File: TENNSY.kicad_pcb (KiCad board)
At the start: 2 copper layers, 120 x 160 mm, 3 parts, among them U1 Teensy4.0

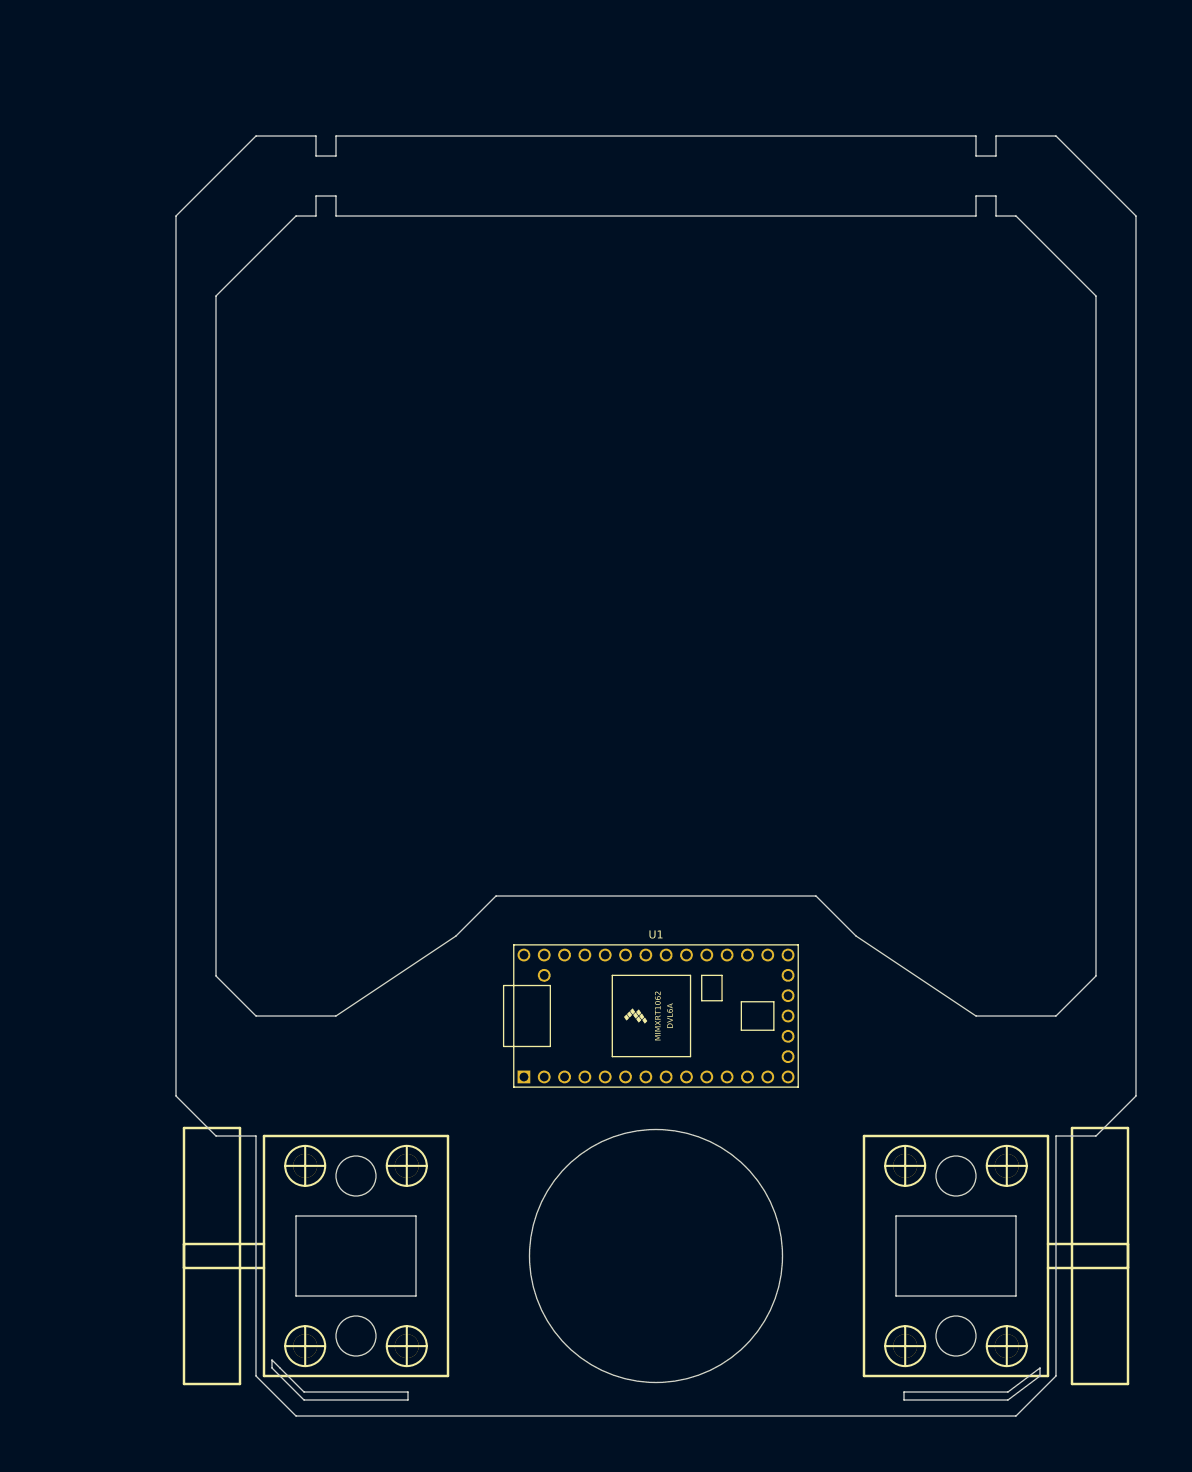
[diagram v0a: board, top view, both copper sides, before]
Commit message: modificaciones
se arego imagenes 3d y modificacion en el sch y pcb
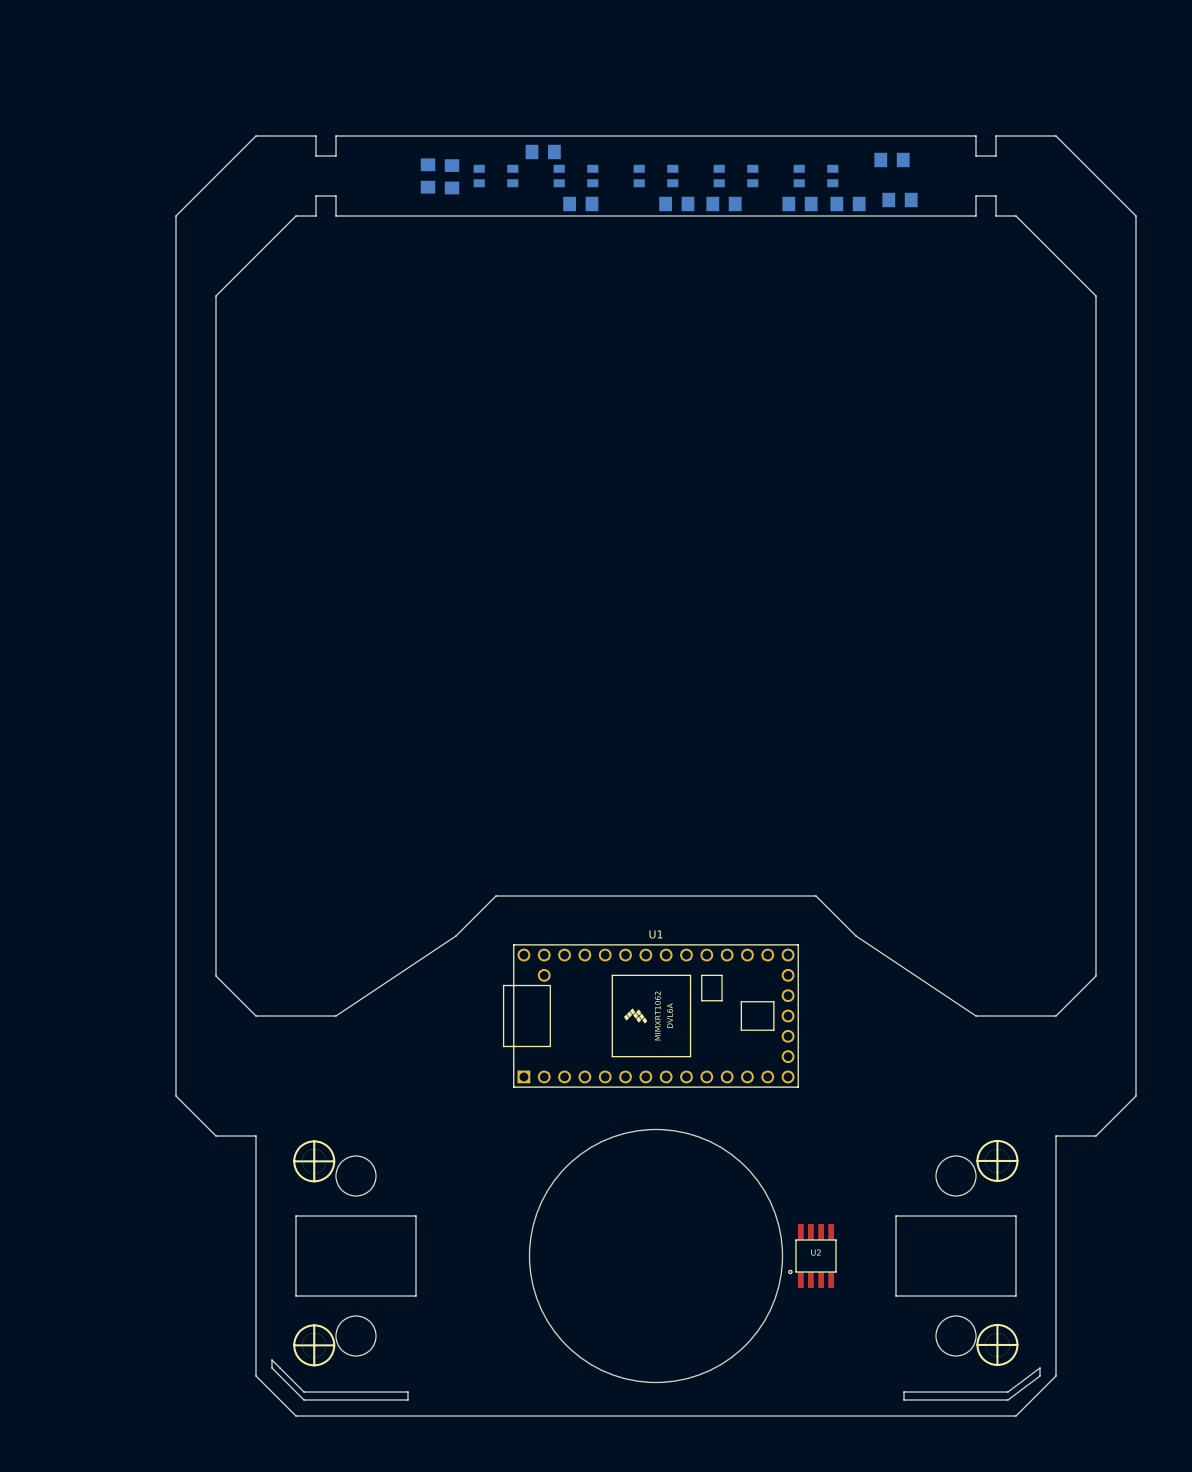
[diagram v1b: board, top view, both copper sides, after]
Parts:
- removed the Pololu_Micro_Gear_Motor at (127.5, 165.0)
- removed the Pololu_Micro_Gear_Motor at (52.5, 165.0)
- added Pololu_Micro_Gear_Motor: VAL**, EESTN5:Pololu_Micro_Con_Soporte_Simple, B.Cu at (47.3, 164.7)
- added Pololu_Micro_Gear_Motor: VAL**, EESTN5:Pololu_Micro_Con_Soporte_Simple, B.Cu at (132.7, 164.6)
- added R1: R, EESTN5:R_1206, B.Cu at (75.9, 27.0)
- added R10: R, EESTN5:R_1206, B.Cu at (120.5, 33.0)
- added R2: R, EESTN5:R_1206, B.Cu at (80.6, 33.5)
- added R3: R, EESTN5:R_1206, B.Cu at (64.5, 30.1)
- added R4: R, EESTN5:R_1206, B.Cu at (61.5, 30.0)
- added R5: R, EESTN5:R_1206, B.Cu at (98.5, 33.5)
- added R6: R, EESTN5:R_1206, B.Cu at (92.6, 33.5)
- added R7: R, EESTN5:R_1206, B.Cu at (114.0, 33.5)
- added R8: R, EESTN5:R_1206, B.Cu at (108.0, 33.5)
- added R9: R, EESTN5:R_1206, B.Cu at (119.5, 28.0)
- added U2: DRV8872, EESTN5:SSOP-8, F.Cu at (110.0, 165.0)
- added U3: QRE1113, EESTN5:QRE1113GR, B.Cu at (80.0, 30.0)
- added U4: QRE1113, EESTN5:QRE1113GR, B.Cu at (70.0, 30.0)
- added U5: QRE1113, EESTN5:QRE1113GR, B.Cu at (90.0, 30.0)
- added U6: QRE1113, EESTN5:QRE1113GR, B.Cu at (100.0, 30.0)
- added U7: QRE1113, EESTN5:QRE1113GR, B.Cu at (110.0, 30.0)
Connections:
- U1 pad 1: Net-(U1-Pad1) -> (no net)
- U1 pad 10: Net-(U1-Pad10) -> (no net)
- U1 pad 11: Net-(U1-Pad11) -> (no net)
- U1 pad 12: Net-(U1-Pad12) -> (no net)
- U1 pad 13: Net-(U1-Pad13) -> (no net)
- U1 pad 14: Net-(U1-Pad14) -> (no net)
- U1 pad 15: Net-(U1-Pad15) -> (no net)
- U1 pad 16: Net-(U1-Pad16) -> (no net)
- U1 pad 17: Net-(U1-Pad17) -> (no net)
- U1 pad 18: Net-(U1-Pad18) -> (no net)
- U1 pad 19: Net-(U1-Pad19) -> (no net)
- U1 pad 2: Net-(U1-Pad2) -> (no net)
- U1 pad 20: Net-(U1-Pad20) -> (no net)
- U1 pad 21: Net-(U1-Pad21) -> (no net)
- U1 pad 22: Net-(U1-Pad22) -> (no net)
- U1 pad 23: Net-(U1-Pad23) -> (no net)
- U1 pad 24: Net-(U1-Pad24) -> (no net)
- U1 pad 25: Net-(U1-Pad25) -> (no net)
- U1 pad 26: Net-(U1-Pad26) -> (no net)
- U1 pad 27: Net-(U1-Pad27) -> (no net)
- U1 pad 28: Net-(U1-Pad28) -> (no net)
- U1 pad 29: Net-(U1-Pad29) -> (no net)
- U1 pad 3: Net-(U1-Pad3) -> (no net)
- U1 pad 30: Net-(U1-Pad30) -> (no net)
- U1 pad 31: Net-(U1-Pad31) -> (no net)
- U1 pad 32: Net-(U1-Pad32) -> (no net)
- U1 pad 33: Net-(U1-Pad33) -> (no net)
- U1 pad 34: Net-(U1-Pad34) -> (no net)
- U1 pad 4: Net-(U1-Pad4) -> (no net)
- U1 pad 5: Net-(U1-Pad5) -> (no net)
- U1 pad 6: Net-(U1-Pad6) -> (no net)
- U1 pad 7: Net-(U1-Pad7) -> (no net)
- U1 pad 8: Net-(U1-Pad8) -> (no net)
- U1 pad 9: Net-(U1-Pad9) -> (no net)

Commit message: modificaciones
se modifico el pcb
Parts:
- R1, R10, R2, R3, R4, R5, R6, R7, R8, R9: moved to F.Cu
- moved R7 16.9 mm to (97.8, 28.6), turned to 90 degrees
- moved R5 11.8 mm to (87.8, 28.6), turned to 90 degrees
- moved R9 11.7 mm to (107.8, 28.6), turned to 90 degrees
- moved R4 10.8 mm to (72.2, 28.6)
- moved R10 9.57 mm to (112.0, 28.6), turned to 90 degrees
- moved R8 7.74 mm to (102.0, 28.6), turned to 90 degrees
- moved R2 5.09 mm to (82.0, 28.6), turned to 90 degrees
- moved R6 4.94 mm to (92.0, 28.6), turned to 90 degrees
- moved R3 3.45 mm to (67.6, 28.6)
- moved R1 2.49 mm to (77.8, 28.6), turned to 90 degrees
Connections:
- R10 pad 2: /5 -> /A0
- R2 pad 2: /2 -> /A3
- R4 pad 2: /1 -> /A6
- R6 pad 2: /3 -> /A2
- R8 pad 2: /4 -> /A1
- U1 pad 1: (no net) -> GND
- U1 pad 17: (no net) -> GND
- U1 pad 21: (no net) -> /A0
- U1 pad 22: (no net) -> /A1
- U1 pad 23: (no net) -> /A2
- U1 pad 24: (no net) -> /A3
- U1 pad 27: (no net) -> /A6
- U1 pad 32: (no net) -> GND
- U3 pad 3: /2 -> /A3
- U4 pad 3: /1 -> /A6
- U5 pad 3: /3 -> /A2
- U6 pad 3: /4 -> /A1
- U7 pad 3: /5 -> /A0
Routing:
- net /A3: track 0.00 -> 226.9 mm, vias 0 -> 1
- net /A2: track 0.00 -> 217.3 mm, vias 0 -> 1
- net /A6: track 0.00 -> 213.5 mm, vias 0 -> 1
- net /A1: track 0.00 -> 207.7 mm, vias 0 -> 1
- net /A0: track 0.00 -> 198.8 mm, vias 0 -> 1
- net +5V: track 0.00 -> 44.4 mm
- net Net-(R7-Pad2): track 0.00 -> 5.62 mm, vias 0 -> 1
- net Net-(R9-Pad2): track 0.00 -> 5.39 mm, vias 0 -> 1
- net Net-(R1-Pad2): track 0.00 -> 5.20 mm, vias 0 -> 1
- net Net-(R3-Pad2): track 0.00 -> 4.96 mm, vias 0 -> 1
- net Net-(R5-Pad2): track 0.00 -> 4.87 mm, vias 0 -> 1
- added copper zone on B.Cu, net GND
- added copper zone on F.Cu, net GND

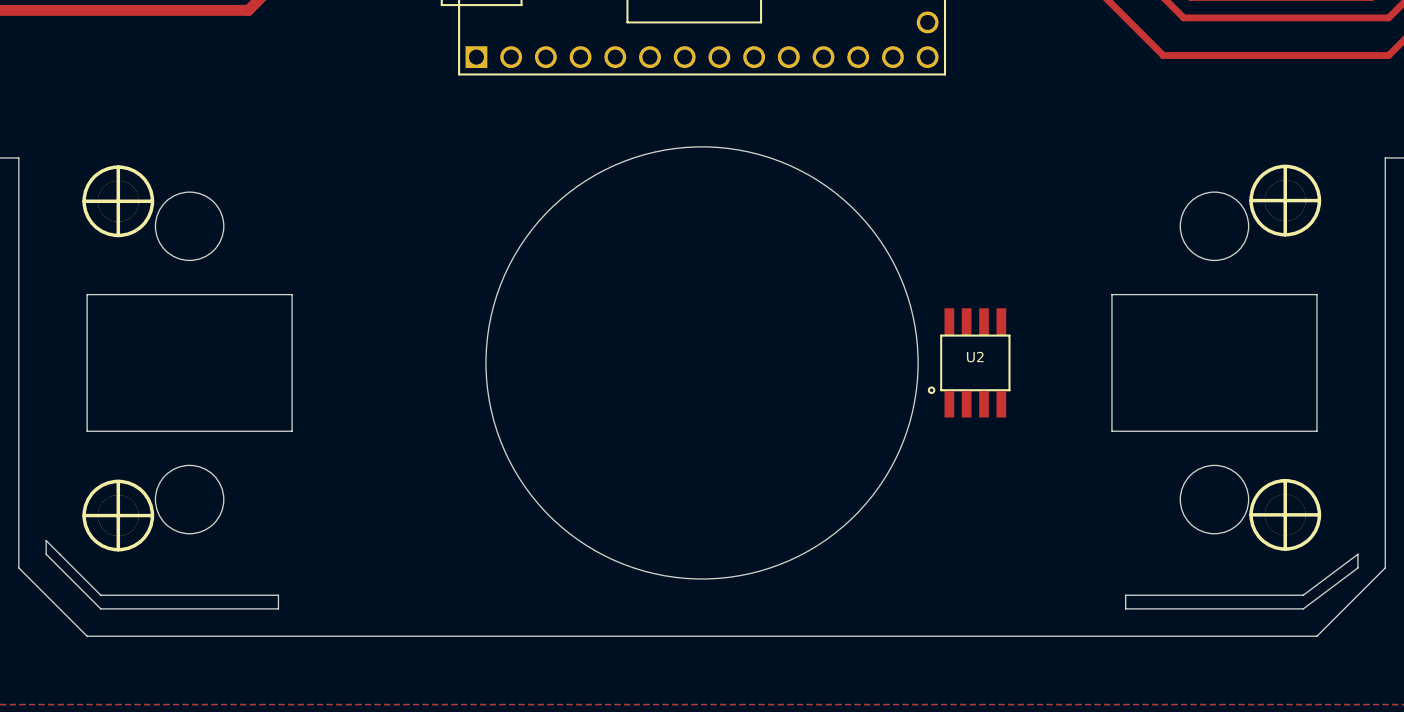
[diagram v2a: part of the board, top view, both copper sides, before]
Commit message: modificaciones
se modifico sch,pcb y se agrego modelos 3d
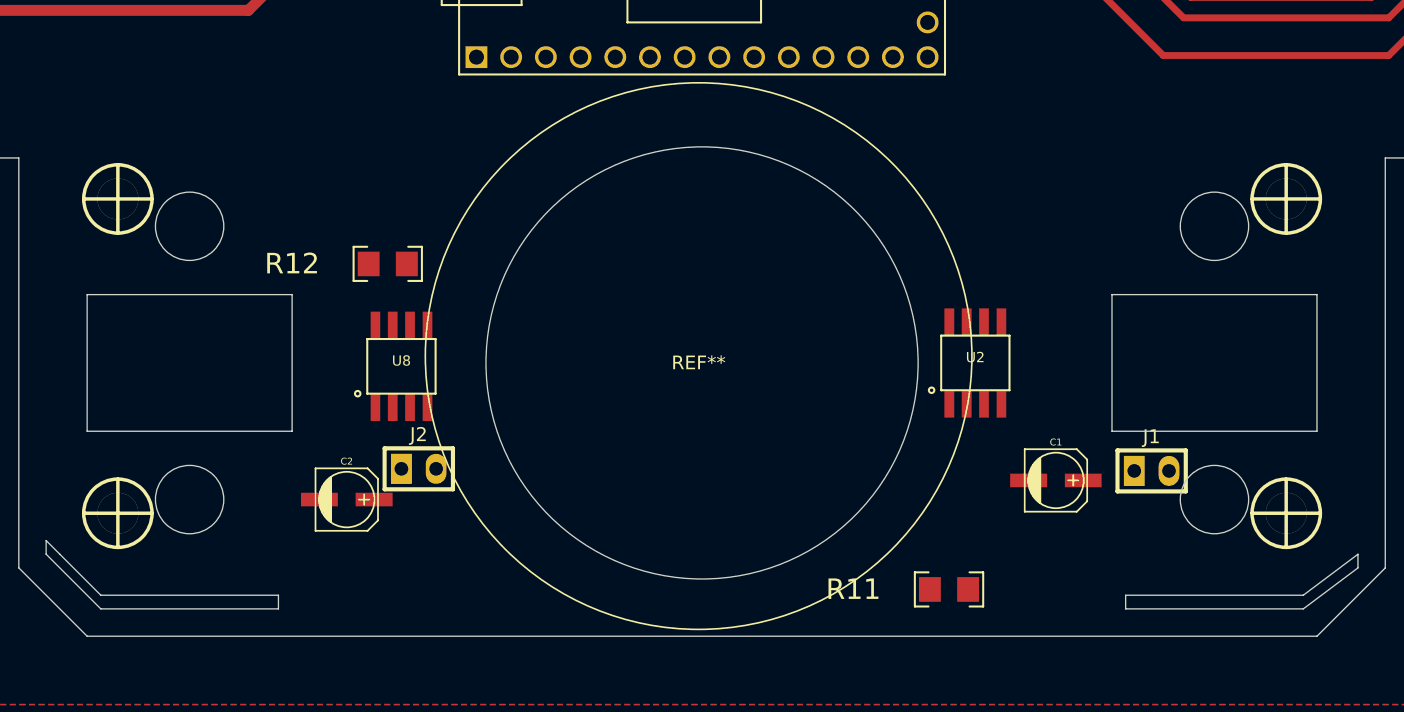
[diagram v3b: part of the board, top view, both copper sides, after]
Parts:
- removed the Pololu_Micro_Gear_Motor at (47.3, 164.7)
- removed the Pololu_Micro_Gear_Motor at (132.7, 164.6)
- added C1: C, EESTN5:CAP_ELEC_SMD_4X5.5, F.Cu at (115.9, 173.6)
- added C2: C, EESTN5:CAP_ELEC_SMD_4X5.5, F.Cu at (64.0, 175.0)
- added J1: HEADER_2, EESTN5:Pin_strip_2, F.Cu at (122.9, 172.9)
- added J2: HEADER_2, EESTN5:Pin_strip_2, F.Cu at (69.3, 172.8)
- added Pololu_Micro_Gear_Motor: VAL**, EESTN5:Pololu_Micro_Con_Soporte_Simple, B.Cu at (132.8, 164.5)
- added Pololu_Micro_Gear_Motor: VAL**, EESTN5:Pololu_Micro_Con_Soporte_Simple, B.Cu at (47.2, 164.5)
- added R11: R, EESTN5:R_1206, F.Cu at (108.1, 181.6)
- added R12: R, EESTN5:R_1206, F.Cu at (67.0, 157.8)
- added REF**: turbina27mm, TEENSY_velocista:turbina27mm, F.Cu at (89.8, 164.5)
- added U8: DRV8872, EESTN5:SSOP-8, F.Cu at (68.0, 165.2)
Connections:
- U2 pad 1: (no net) -> GND
- U2 pad 5: (no net) -> /VIN
- U2 pad 6: (no net) -> Net-(J1-Pad2)
- U2 pad 7: (no net) -> Net-(R11-Pad1)
- U2 pad 8: (no net) -> Net-(J1-Pad1)
